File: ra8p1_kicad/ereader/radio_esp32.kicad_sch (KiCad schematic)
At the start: 19 parts, among them U3 ESP32-C6-WROOM-1-N8, U4 TPS22917DBVT, U5 TXU0304PWR, U6 TPS389001DSET

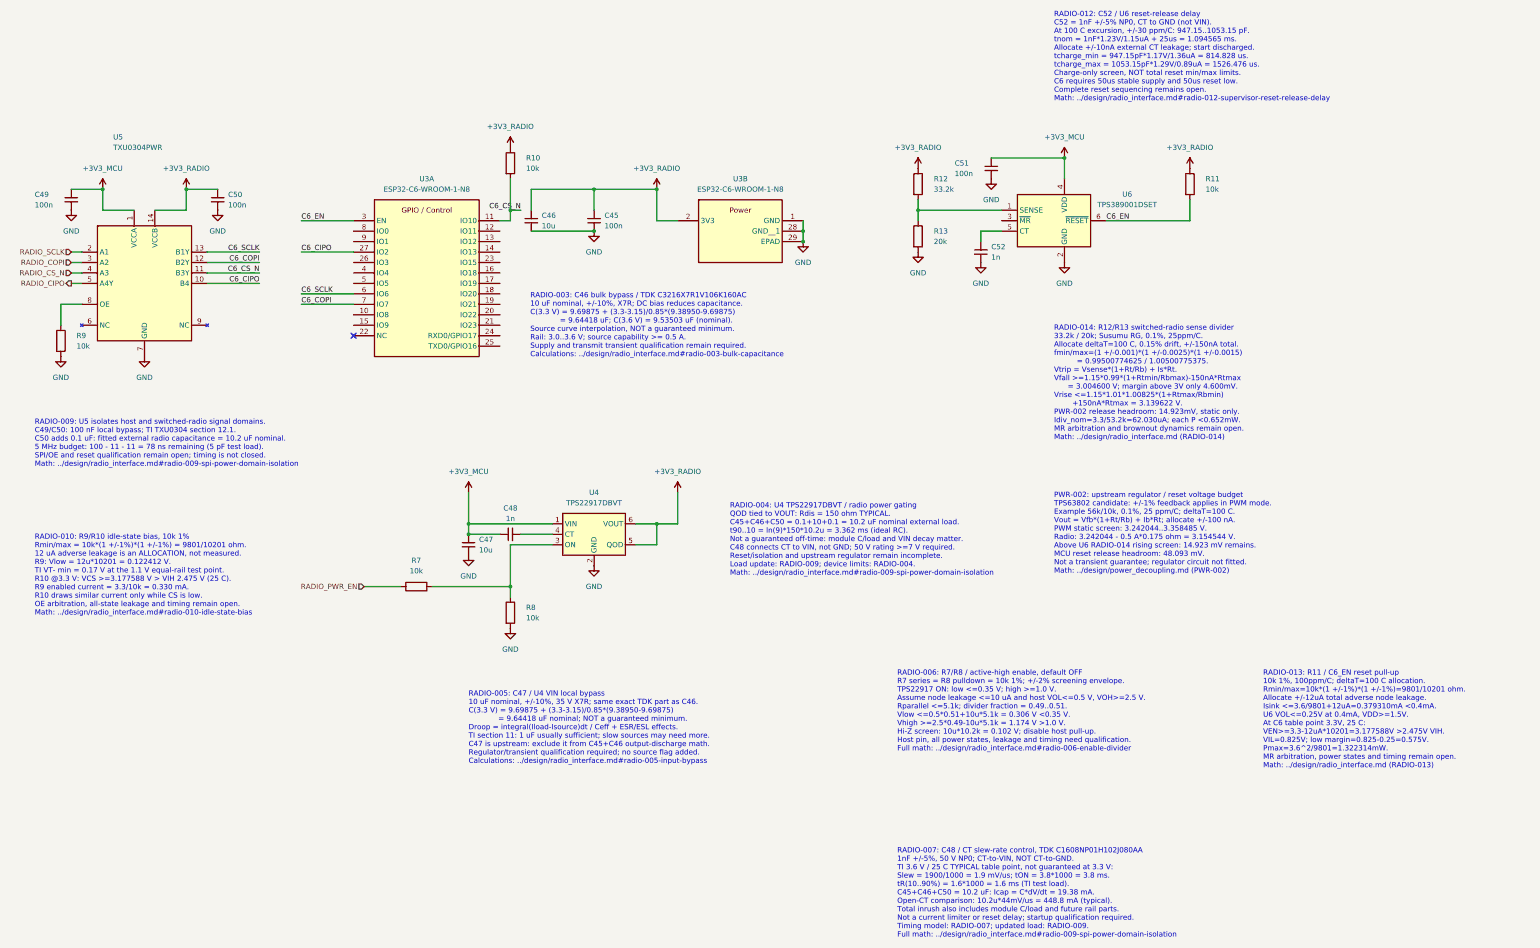
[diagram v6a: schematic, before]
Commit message: Add radio reset arbitration gate and documented bias circuit
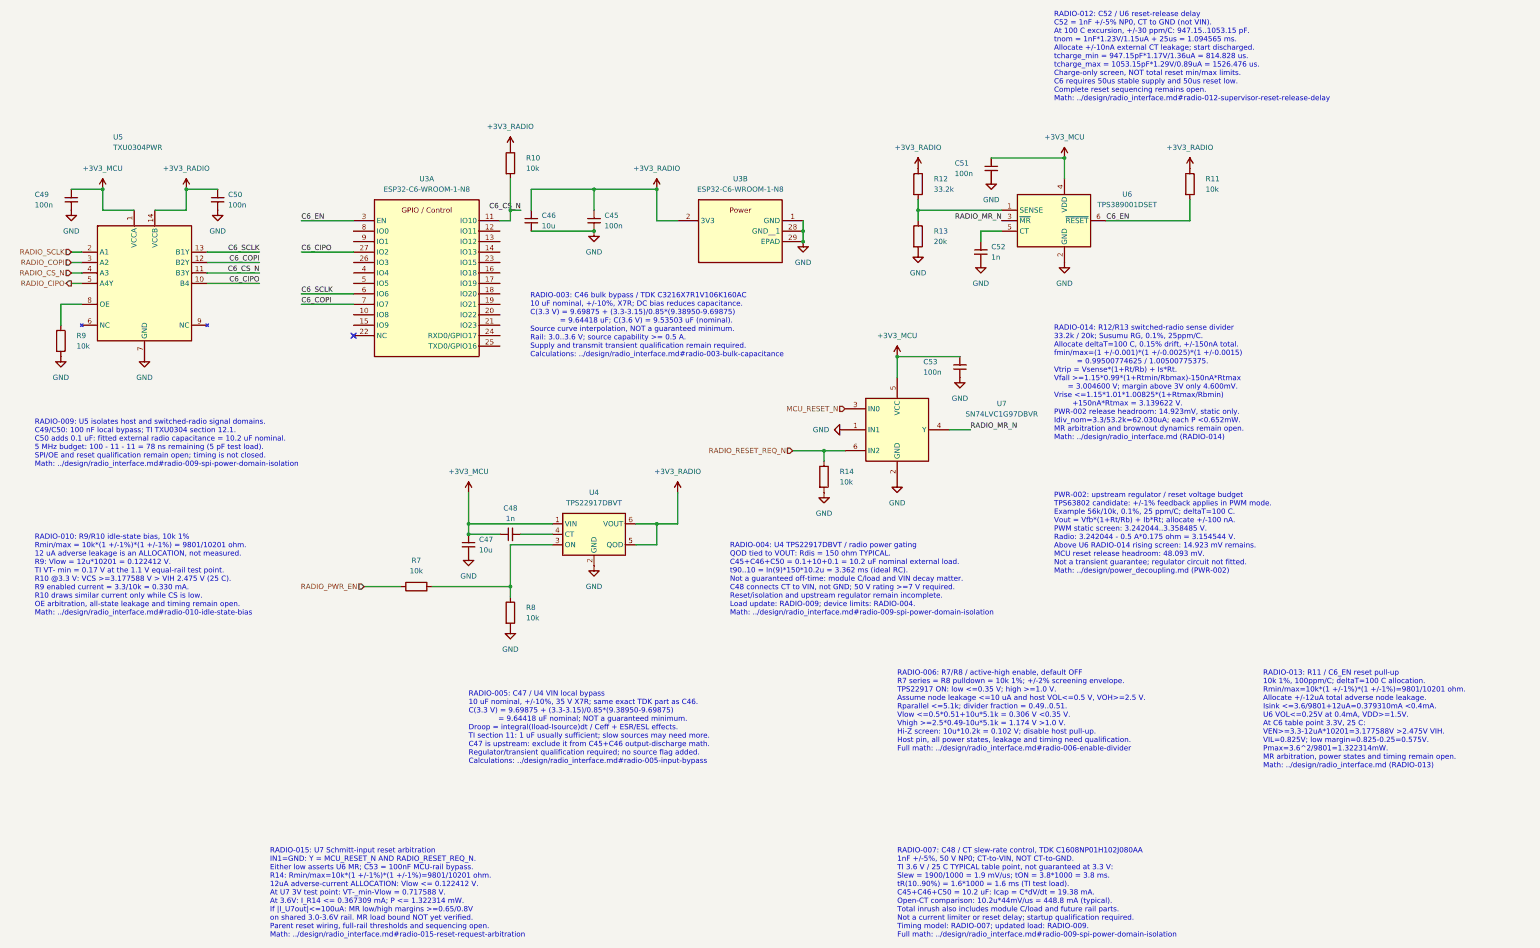
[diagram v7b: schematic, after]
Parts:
- added C53: 100n, symbol Device:C_Small
- added R14: 10k, symbol Device:R
- added U7: SN74LVC1G97DBVR, symbol 74xGxx:74LVC1G97
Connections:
- net +3V3_MCU: now also C53.1, U7.5 (VCC)
- net GND: now also C53.2, R14.2, U7.1 (IN1), U7.2 (GND)
- net RADIO_MR_N: now reaches U6.3 (~{MR})
- net RADIO_MR_N: now also U7.4 (Y)
- new net MCU_RESET_N: U7.3 (IN0)
- new net RADIO_RESET_REQ_N: R14.1, U7.6 (IN2)
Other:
- note added: "RADIO-015: U7 Schmitt-input reset arbitration IN1=GND: Y = MCU_RESET_N AND RADIO_RESET_REQ_N. Either low asserts U6 MR; C53 = 100nF MCU-rail bypass. R14: Rmin/max=10k*(1 +/-1%)*(1 +/-1%)=9801/10201 ohm. 12uA adverse-current ALLOCATION: Vlow <= 0.122412 V. At U7 3V test point: VT-_min-Vlow = 0.717588 V. At 3.6V: I_R14 <= 0.367309 mA; P <= 1.322314 mW. If |I_U7out|<=100uA: MR low/high margins >=0.6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"

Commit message: Connect radio reset controls through schematic hierarchy
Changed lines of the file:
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@@
 		)
 	)
-	(text "RADIO-015: U7 Schmitt-input reset arbitration\nIN1=GND: Y = MCU_RESET_N AND RADIO_RESET_REQ_N.\nEither low asserts U6 MR; C53 = 100nF MCU-rail bypass.\nR14: Rmin/max=10k*(1 +/-1%)*(1 +/-1%)=9801/10201 ohm.\n12uA adverse-current ALLOCATION: Vlow <= 0.122412 V.\nAt U7 3V test point: VT-_min-Vlow = 0.717588 V.\nAt 3.6V: I_R14 <= 0.367309 mA; P <= 1.322314 mW.\nIf |I_U7out|<=100uA: MR low/high margins >=0.65/0.8V\non shared 3.0-3.6V rail. MR load bound NOT yet verified.\nParent reset wiring, full-rail thresholds and sequencing open.\nMath: ../design/radio_interface.md#radio-015-reset-request-arbitration"
+	(text "RADIO-015: U7 Schmitt-input reset arbitration\nIN1=GND: Y = MCU_RESET_N AND RADIO_RESET_REQ_N.\nEither low asserts U6 MR; C53 = 100nF MCU-rail bypass.\nR14: Rmin/max=10k*(1 +/-1%)*(1 +/-1%)=9801/10201 ohm.\n12uA adverse-current ALLOCATION: Vlow <= 0.122412 V.\nAt U7 3V test point: VT-_min-Vlow = 0.717588 V.\nAt 3.6V: I_R14 <= 0.367309 mA; P <= 1.322314 mW.\nIf |I_U7out|<=100uA: MR low/high margins >=0.65/0.8V\non shared 3.0-3.6V rail. MR load bound NOT yet verified.\nReset hierarchy connected; full-rail thresholds/sequencing open.\nMath: ../design/radio_interface.md#radio-015-reset-request-arbitration"
 		(exclude_from_sim no)
 		(at 76.2 228.6 0)
